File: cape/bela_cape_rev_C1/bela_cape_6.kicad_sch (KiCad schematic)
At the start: 48 parts, among them IC3 ES9080Q, J12 Conn_01x03, J13 Conn_01x03, J14 Conn_01x03, J15 Conn_01x03, U1 TL974, U2 TL974

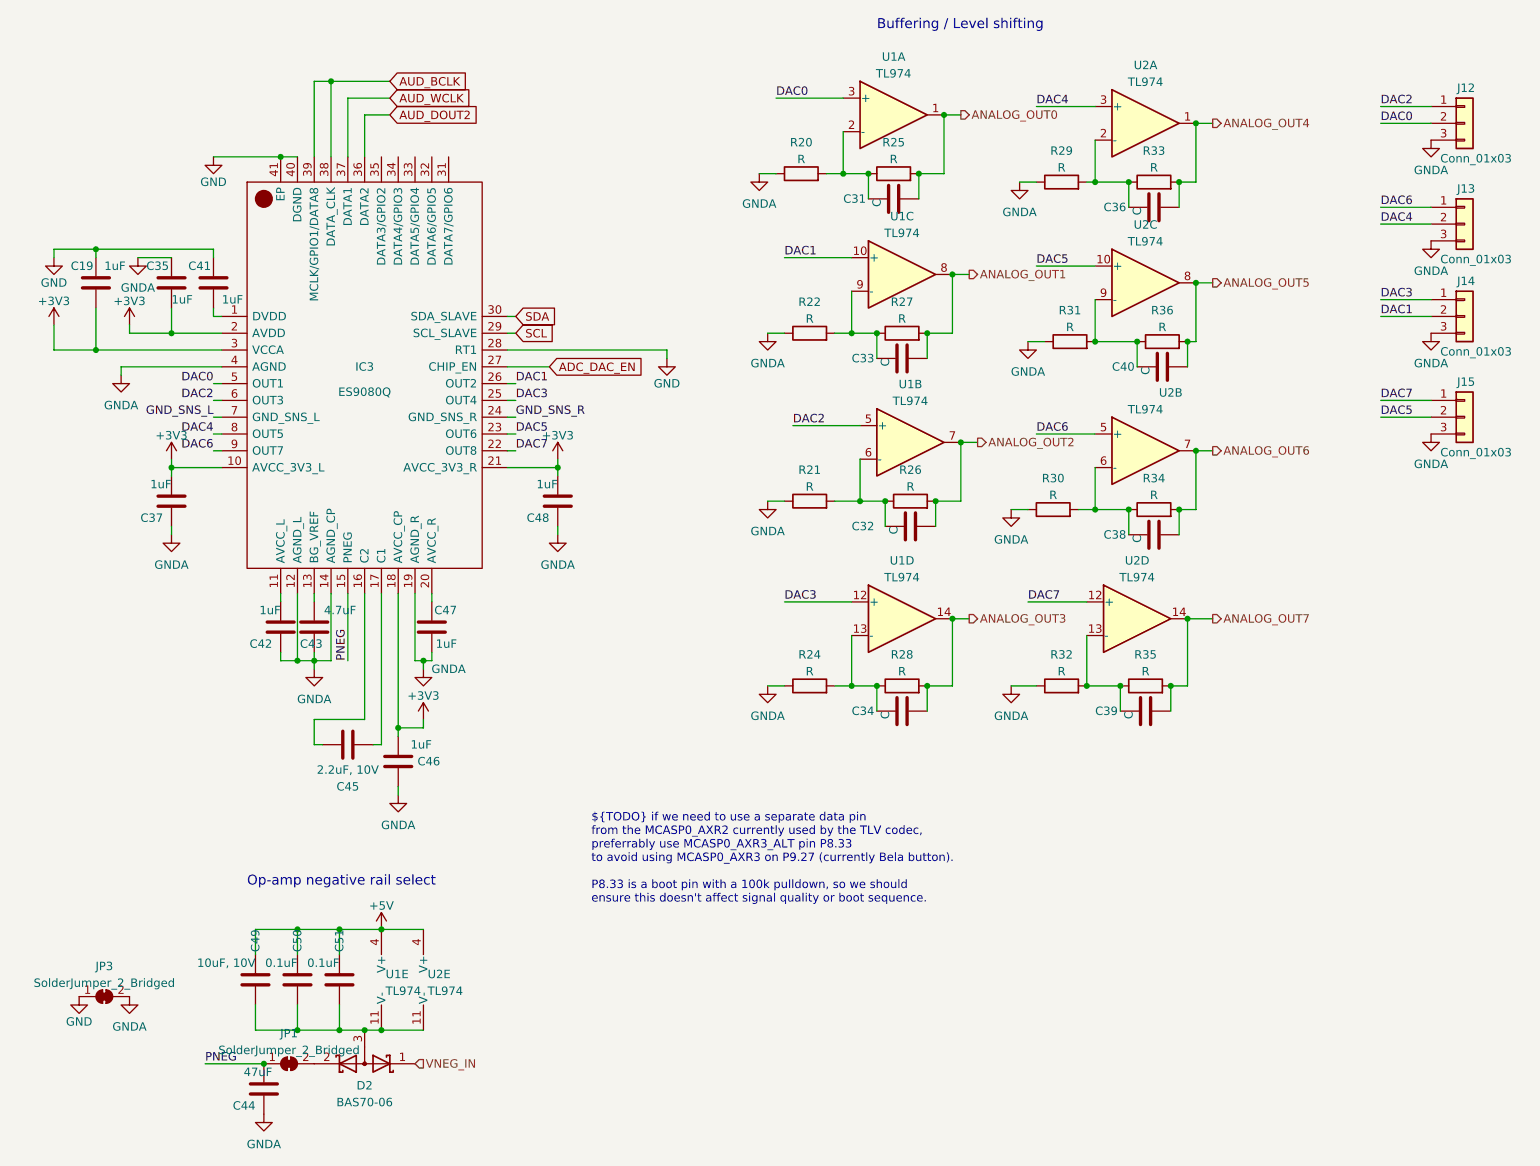
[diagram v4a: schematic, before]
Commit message: C1 cape: clean up bottom silkscreen
(cherry picked from commit 7c02b20f8f7a862246e5856b6fa8015b8ad6464b)
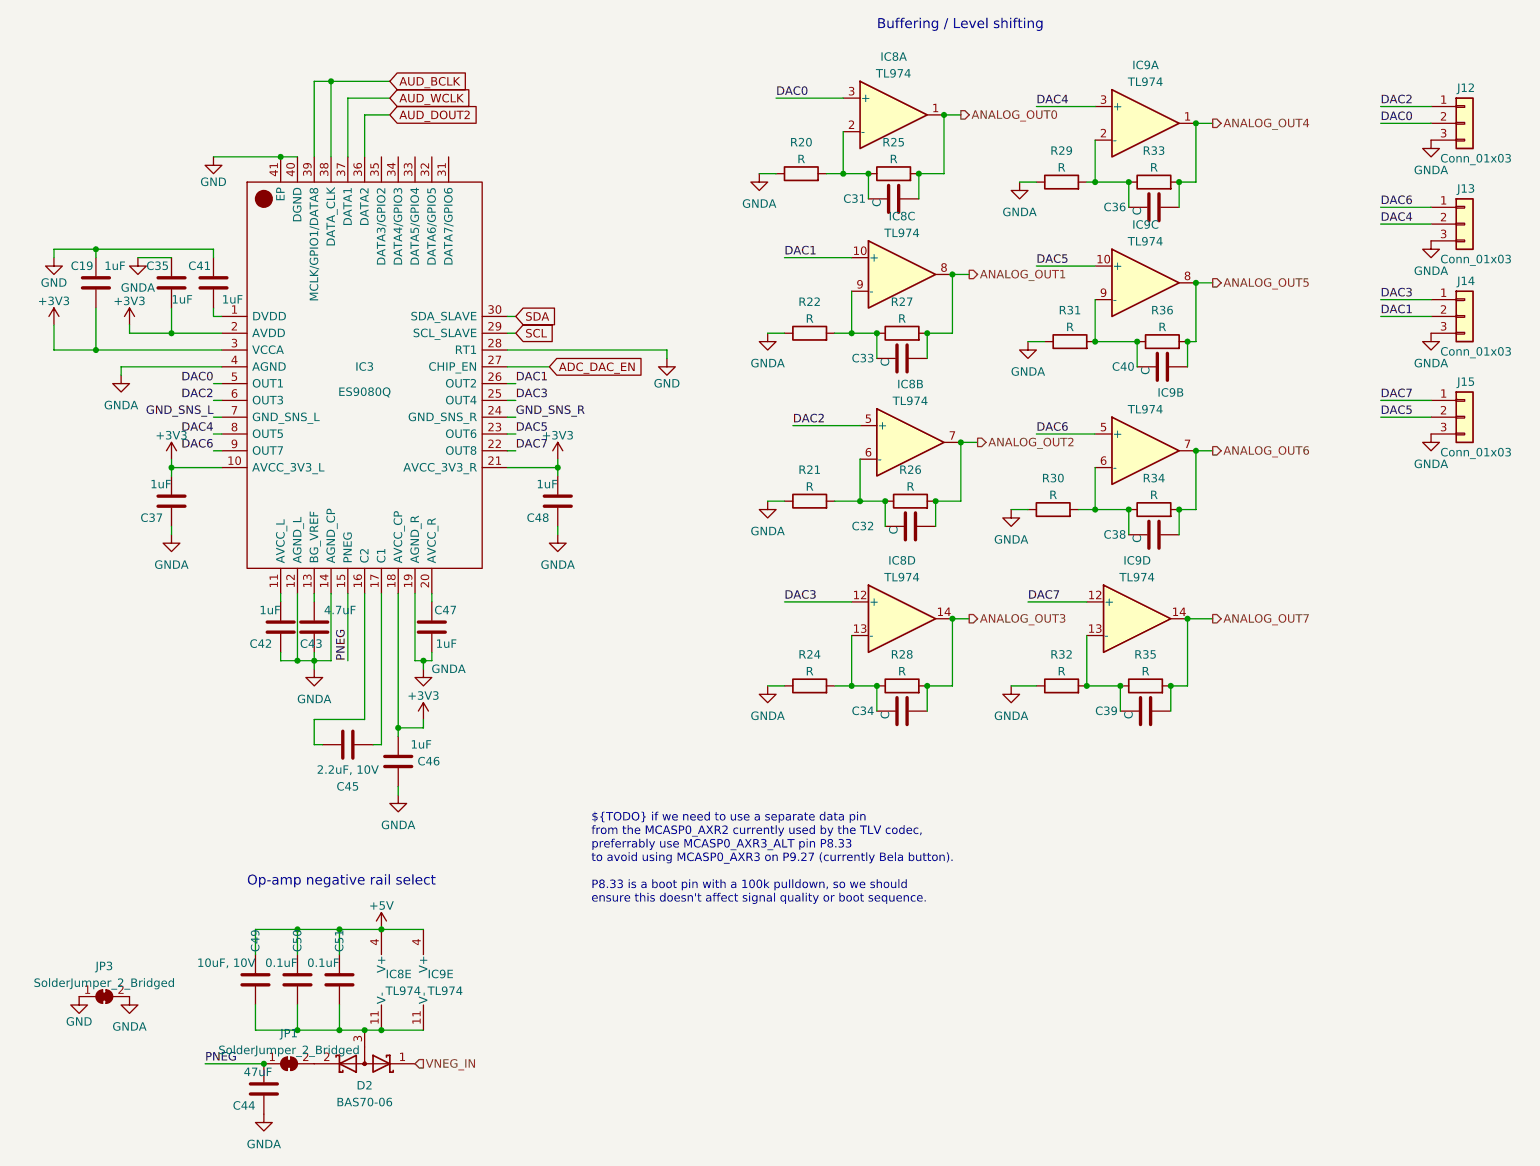
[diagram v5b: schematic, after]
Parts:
- renumbered U1 to IC8, U2 to IC9
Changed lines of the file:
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@@
   (symbol (lib_id "Amplifier_Operational:TL074") (at 191.77 33.02 0) (unit 1)
     (in_bom yes) (on_board yes) (fields_autoplaced)
-    (property "Reference" "U2" (id 0) (at 191.77 24.2402 0))
+    (property "Reference" "IC9" (id 0) (at 191.77 24.2402 0))
     (property "Value" "TL974" (id 1) (at 191.77 26.7771 0))
     (property "Footprint" "Package_SO:TSSOP-14_4.4x5mm_P0.65mm" (id 2) (at 190.5 30.48 0)
@@
   (symbol (lib_id "Amplifier_Operational:TL074") (at 154.94 107.95 0) (unit 4)
     (in_bom yes) (on_board yes) (fields_autoplaced)
-    (property "Reference" "U1" (id 0) (at 154.94 99.1702 0))
+    (property "Reference" "IC8" (id 0) (at 154.94 99.1702 0))
     (property "Value" "TL974" (id 1) (at 154.94 101.7071 0))
     (property "Footprint" "Package_SO:TSSOP-14_4.4x5mm_P0.65mm" (id 2) (at 153.67 105.41 0)
@@
   (symbol (lib_id "Amplifier_Operational:TL074") (at 153.67 31.75 0) (unit 1)
     (in_bom yes) (on_board yes) (fields_autoplaced)
-    (property "Reference" "U1" (id 0) (at 153.67 22.9702 0))
+    (property "Reference" "IC8" (id 0) (at 153.67 22.9702 0))
     (property "Value" "TL974" (id 1) (at 153.67 25.5071 0))
     (property "Footprint" "Package_SO:TSSOP-14_4.4x5mm_P0.65mm" (id 2) (at 152.4 29.21 0)
@@
   (symbol (lib_id "Amplifier_Operational:TL074") (at 191.77 57.15 0) (unit 3)
     (in_bom yes) (on_board yes) (fields_autoplaced)
-    (property "Reference" "U2" (id 0) (at 191.77 48.3702 0))
+    (property "Reference" "IC9" (id 0) (at 191.77 48.3702 0))
     (property "Value" "TL974" (id 1) (at 191.77 50.9071 0))
     (property "Footprint" "Package_SO:TSSOP-14_4.4x5mm_P0.65mm" (id 2) (at 190.5 54.61 0)
@@
   (symbol (lib_id "Amplifier_Operational:TL074") (at 78.74 162.56 0) (unit 5)
     (in_bom yes) (on_board yes) (fields_autoplaced)
-    (property "Reference" "U1" (id 0) (at 76.835 161.7253 0)
+    (property "Reference" "IC8" (id 0) (at 76.835 161.7253 0)
       (effects (font (size 1.27 1.27)) (justify left))
     )
@@
   (symbol (lib_id "Amplifier_Operational:TL074") (at 85.09 162.56 0) (unit 5)
     (in_bom yes) (on_board yes) (fields_autoplaced)
-    (property "Reference" "U2" (id 0) (at 83.185 161.7253 0)
+    (property "Reference" "IC9" (id 0) (at 83.185 161.7253 0)
       (effects (font (size 1.27 1.27)) (justify left))
     )
@@
   (symbol (lib_id "Amplifier_Operational:TL074") (at 190.5 107.95 0) (unit 4)
     (in_bom yes) (on_board yes) (fields_autoplaced)
-    (property "Reference" "U2" (id 0) (at 190.5 99.1702 0))
+    (property "Reference" "IC9" (id 0) (at 190.5 99.1702 0))
     (property "Value" "TL974" (id 1) (at 190.5 101.7071 0))
     (property "Footprint" "Package_SO:TSSOP-14_4.4x5mm_P0.65mm" (id 2) (at 189.23 105.41 0)
@@
   (symbol (lib_id "Amplifier_Operational:TL074") (at 156.21 81.28 0) (unit 2)
     (in_bom yes) (on_board yes) (fields_autoplaced)
-    (property "Reference" "U1" (id 0) (at 156.21 72.5002 0))
+    (property "Reference" "IC8" (id 0) (at 156.21 72.5002 0))
     (property "Value" "TL974" (id 1) (at 156.21 75.0371 0))
     (property "Footprint" "Package_SO:TSSOP-14_4.4x5mm_P0.65mm" (id 2) (at 154.94 78.74 0)
@@
   (symbol (lib_id "Amplifier_Operational:TL074") (at 191.77 82.55 0) (unit 2)
     (in_bom yes) (on_board yes)
-    (property "Reference" "U2" (id 0) (at 195.58 73.7702 0))
+    (property "Reference" "IC9" (id 0) (at 195.58 73.7702 0))
     (property "Value" "TL974" (id 1) (at 191.77 76.3071 0))
     (property "Footprint" "Package_SO:TSSOP-14_4.4x5mm_P0.65mm" (id 2) (at 190.5 80.01 0)
@@
   (symbol (lib_id "Amplifier_Operational:TL074") (at 154.94 55.88 0) (unit 3)
     (in_bom yes) (on_board yes) (fields_autoplaced)
-    (property "Reference" "U1" (id 0) (at 154.94 47.1002 0))
+    (property "Reference" "IC8" (id 0) (at 154.94 47.1002 0))
     (property "Value" "TL974" (id 1) (at 154.94 49.6371 0))
     (property "Footprint" "Package_SO:TSSOP-14_4.4x5mm_P0.65mm" (id 2) (at 153.67 53.34 0)

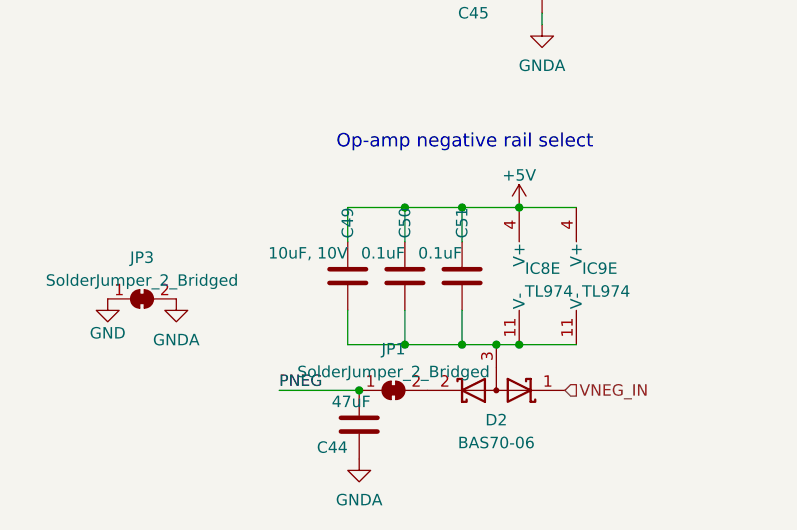
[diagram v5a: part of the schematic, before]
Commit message: Further C1 cape updates
(cherry picked from commit 4c76e949636c5b1483c5ffba2ecc0f217292ab87)
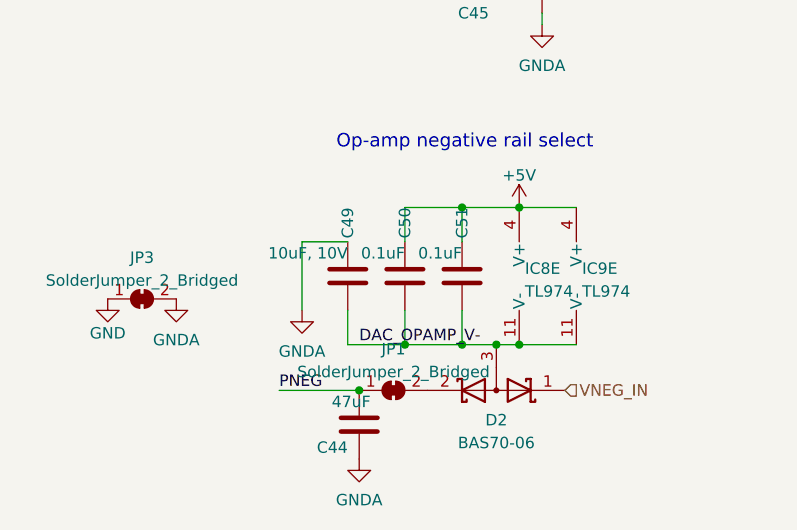
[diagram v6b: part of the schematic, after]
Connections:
- net +5V: no longer C49.2
- net GNDA: now also C49.2
- net DAC_OPAMP_V-: now reaches C49.1, C50.1, C51.1, D2.3 (A), IC8.11 (V-), IC9.11 (V-)
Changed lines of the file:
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@@
   (junction (at 44.45 64.77) (diameter 0) (color 0 0 0 0)
   )
-  (junction (at 63.5 154.94) (diameter 0) (color 0 0 0 0)
-  )
   (junction (at 76.2 170.18) (diameter 0) (color 0 0 0 0)
   )
@@
     (stroke (width 0) (type default) (color 0 0 0 0))
   )
-  (wire (pts (xy 63.5 154.94) (xy 57.15 154.94))
-    (stroke (width 0) (type default) (color 0 0 0 0))
-  )
   (wire (pts (xy 227.33 59.69) (xy 234.95 59.69))
     (stroke (width 0) (type default) (color 0 0 0 0))
@@
     (stroke (width 0) (type default) (color 0 0 0 0))
   )
-  (wire (pts (xy 57.15 154.94) (xy 57.15 158.75))
-    (stroke (width 0) (type default) (color 0 0 0 0))
-  )
   (wire (pts (xy 26.67 67.31) (xy 33.02 67.31))
     (stroke (width 0) (type default) (color 0 0 0 0))
@@
     (stroke (width 0) (type default) (color 0 0 0 0))
   )
+  (wire (pts (xy 57.15 158.75) (xy 52.07 158.75))
+    (stroke (width 0) (type default) (color 0 0 0 0))
+  )
   (wire (pts (xy 81.28 104.14) (xy 81.28 114.3))
     (stroke (width 0) (type default) (color 0 0 0 0))
@@
   )
   (wire (pts (xy 66.04 115.57) (xy 66.04 114.3))
+    (stroke (width 0) (type default) (color 0 0 0 0))
+  )
+  (wire (pts (xy 52.07 158.75) (xy 52.07 166.37))
     (stroke (width 0) (type default) (color 0 0 0 0))
   )
@@
   )
   (label "DAC1" (at 227.33 62.23 0)
+    (effects (font (size 1.27 1.27)) (justify left bottom))
+  )
+  (label "DAC_OPAMP_V-" (at 58.42 170.18 0)
     (effects (font (size 1.27 1.27)) (justify left bottom))
   )
@@
     (pin "2")
   )
+  (symbol (lib_id "power:GNDA") (at 52.07 166.37 0) (unit 1)
+    (in_bom yes) (on_board yes)
+    (property "Reference" "#PWR0175" (id 0) (at 52.07 172.72 0)
+      (effects (font (size 1.27 1.27)) hide)
+    )
+    (property "Value" "GNDA" (id 1) (at 52.07 170.9325 0))
+    (property "Footprint" "" (id 2) (at 52.07 166.37 0)
+      (effects (font (size 1.27 1.27)) hide)
+    )
+    (property "Datasheet" "" (id 3) (at 52.07 166.37 0)
+      (effects (font (size 1.27 1.27)) hide)
+    )
+    (pin "1")
+  )
   (symbol (lib_id "power:GNDA") (at 172.72 41.91 0) (unit 1)
